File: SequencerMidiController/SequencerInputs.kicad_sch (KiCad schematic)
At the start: 35 parts, among them SW2 SW_SPDT-2MS1T1B1M2QES, SW4 SW_DIP_x04, SW5 SW_SPST, U35 ADP5587-ACPZ_LFCSP24, U36 TLC5955DCA_HTSSOP56, U37 TLC5955DCA_HTSSOP56

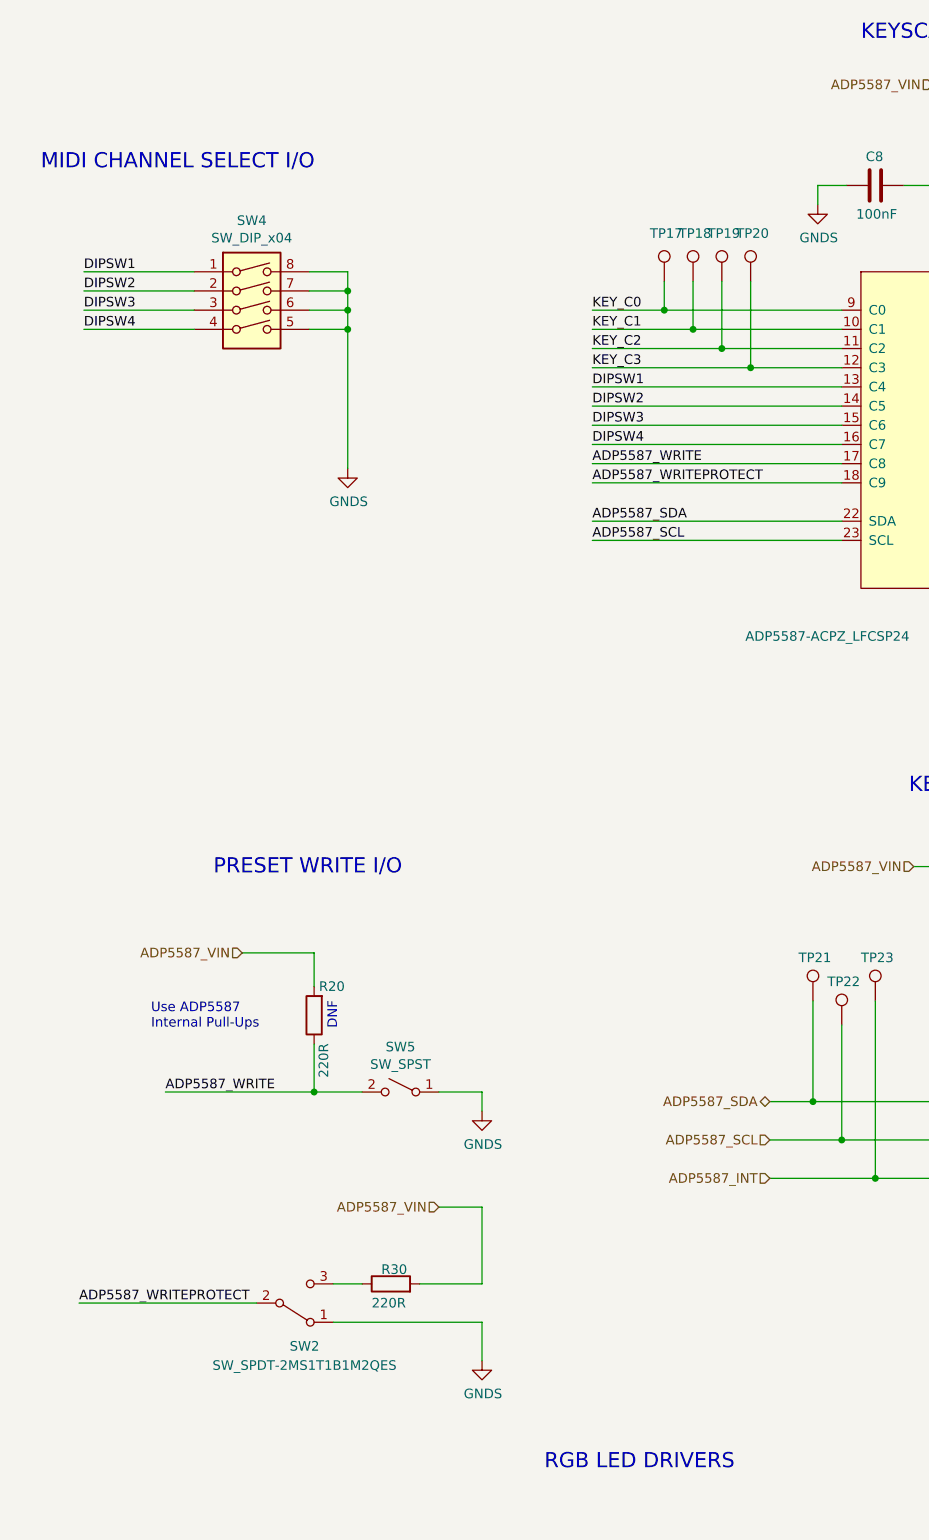
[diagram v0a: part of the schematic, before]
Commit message: updated user buttons
removed dipsw, added four more tactile button (three above display, three below display, six total)
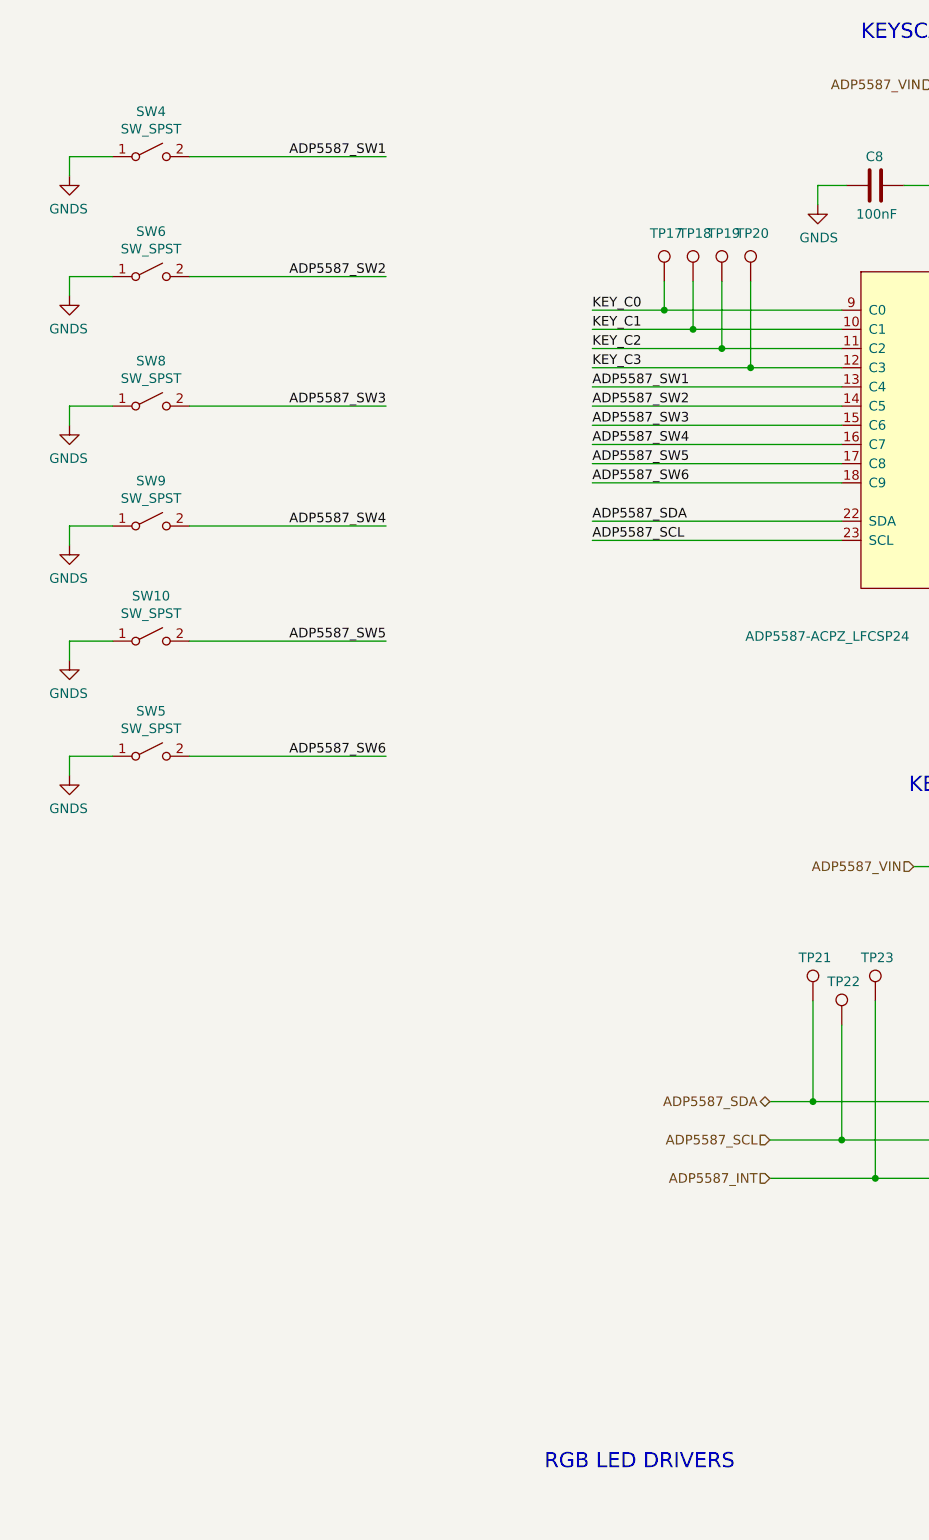
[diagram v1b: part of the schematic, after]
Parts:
- removed R20, R30: 220R, Resistor_SMD:R_0805_2012Metric_Pad1.20x1.40mm_HandSolder, symbol Device:R
- removed SW2: SW_SPDT-2MS1T1B1M2QES, DailywellSwitches:Dailywell_SPDT, symbol Switch:SW_SPDT
- removed SW4: SW_DIP_x04, Button_Switch_THT:SW_DIP_SPSTx04_Slide_9.78x12.34mm_W7.62mm_P2.54mm, symbol Switch:SW_DIP_x04
- added SW10, SW4, SW6, SW8, SW9: SW_SPST, Button_Switch_THT:SW_PUSH-12mm, symbol Switch:SW_SPST
- U35: footprint Package_CSP:LFCSP-24-1EP_4x4mm_P0.5mm_EP2.3x2.3mm_ThermalVias -> Package_CSP:LFCSP-24-1EP_4x4mm_P0.5mm_EP2.3x2.3mm
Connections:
- net GNDS: now also SW10.1 (A), SW4.1 (A), SW6.1 (A), SW8.1 (A), SW9.1 (A)
- net ADP5587_WRITE renamed ADP5587_SW5
- net ADP5587_SW5: now also SW10.2 (B); no longer SW5.2 (B)
- net ADP5587_WRITEPROTECT renamed ADP5587_SW6
- net ADP5587_SW6: now also SW5.2 (B)
- net DIPSW1 renamed ADP5587_SW1
- net ADP5587_SW1: now also SW4.2 (B)
- net DIPSW2 renamed ADP5587_SW2
- net ADP5587_SW2: now also SW6.2 (B)
- net DIPSW3 renamed ADP5587_SW3
- net ADP5587_SW3: now also SW8.2 (B)
- net DIPSW4 renamed ADP5587_SW4
- net ADP5587_SW4: now also SW9.2 (B)
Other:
- note removed: "DNF"
- note removed: "MIDI CHANNEL SELECT I/O"
- note removed: "PRESET WRITE I/O"
- note removed: "Use ADP5587 Internal Pull-Ups"
- moved on the sheet: SW5
